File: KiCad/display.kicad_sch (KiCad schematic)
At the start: 34 parts, among them IC2 R1200N001A-TR-FE, J3 Conn_01x34_NHD_18, Q4 DMG2302U, U6 LT1963AxST-2.5

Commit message: Create Revision 0.0.1
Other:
- company: (none) -> ETH Zurich: Center for Project Based Learning
- title: (none) -> STDC: Display
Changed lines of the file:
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@@
 	(generator_version "9.0")
 	(paper "A4")
+	(title_block
+		(title "STDC: Display")
+		(date "2026-03-05")
+		(rev "0.0.1")
+		(company "ETH Zurich: Center for Project Based Learning")
+	)
 	(rectangle
 		(start 71.12 15.24)

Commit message: Added some TODOs, fixed some TODOs
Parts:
- renumbered C14 to C48, C48 to C49
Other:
- note added: "TODO: Check Peak Saturation Current through L4"
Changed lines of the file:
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@@
 		)
 	)
+	(text "TODO: Check Peak \nSaturation Current\nthrough L4"
+		(exclude_from_sim no)
+		(at 242.57 95.758 0)
+		(effects
+			(font
+				(size 1.27 1.27)
+			)
+		)
+	)
 	(text "1.8V with Power Decoupling\nfor Display VDDIO"
 		(exclude_from_sim no)
@@
 	(text "V_{out}=V_{FB}×(R1+R2)/R1\nV_{FB} = 1.238\n(17/1.238)=13.73\nR2=12.73×R1\n(200k/16k)=12.5"
 		(exclude_from_sim no)
-		(at 242.316 84.582 0)
+		(at 242.062 83.058 0)
 		(effects
 			(font
@@
 		(on_board yes)
 		(dnp no)
-		(property "Reference" "C14"
+		(property "Reference" "C48"
 			(at 212.598 80.518 0)
 			(effects
@@
 			(project ""
 				(path "/643c756f-a801-466b-9148-7370ee6a5e00/603cffac-84d5-485b-bf95-e3987997ef84"
-					(reference "C14")
+					(reference "C48")
 					(unit 1)
 				)
@@
 		(on_board yes)
 		(dnp no)
-		(property "Reference" "C48"
+		(property "Reference" "C49"
 			(at 222.504 80.518 0)
 			(effects
@@
 			(project "STDC"
 				(path "/643c756f-a801-466b-9148-7370ee6a5e00/603cffac-84d5-485b-bf95-e3987997ef84"
-					(reference "C48")
+					(reference "C49")
 					(unit 1)
 				)

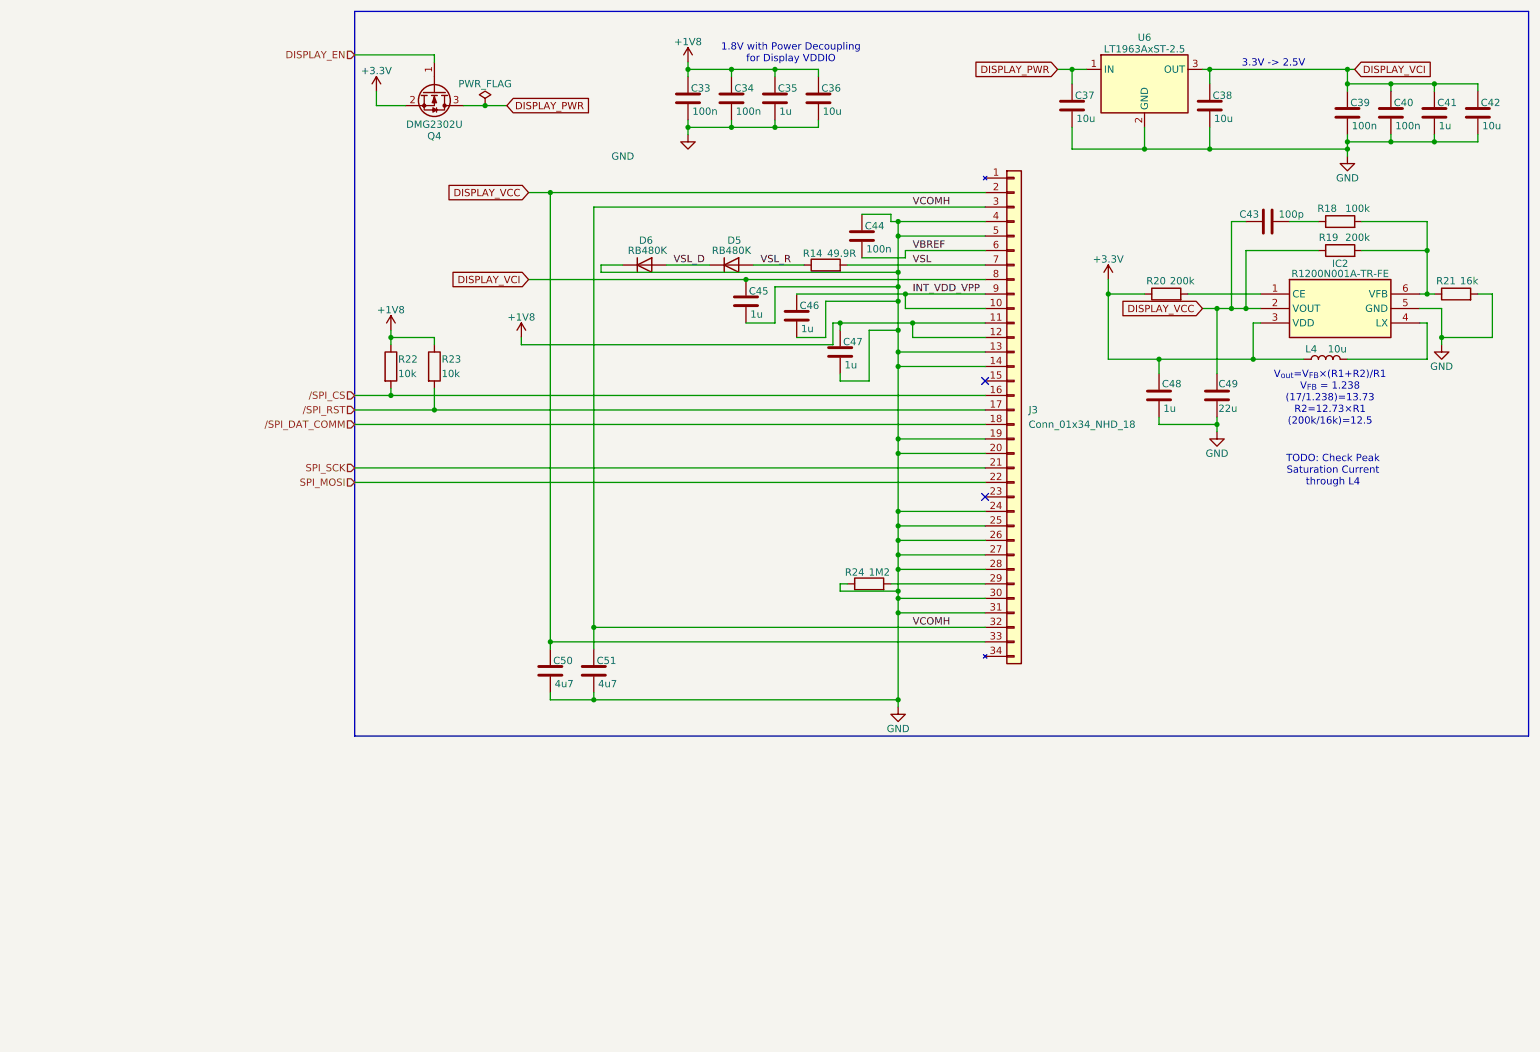
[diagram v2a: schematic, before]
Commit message: Testing connectors, SPI2 pinout, reannotate
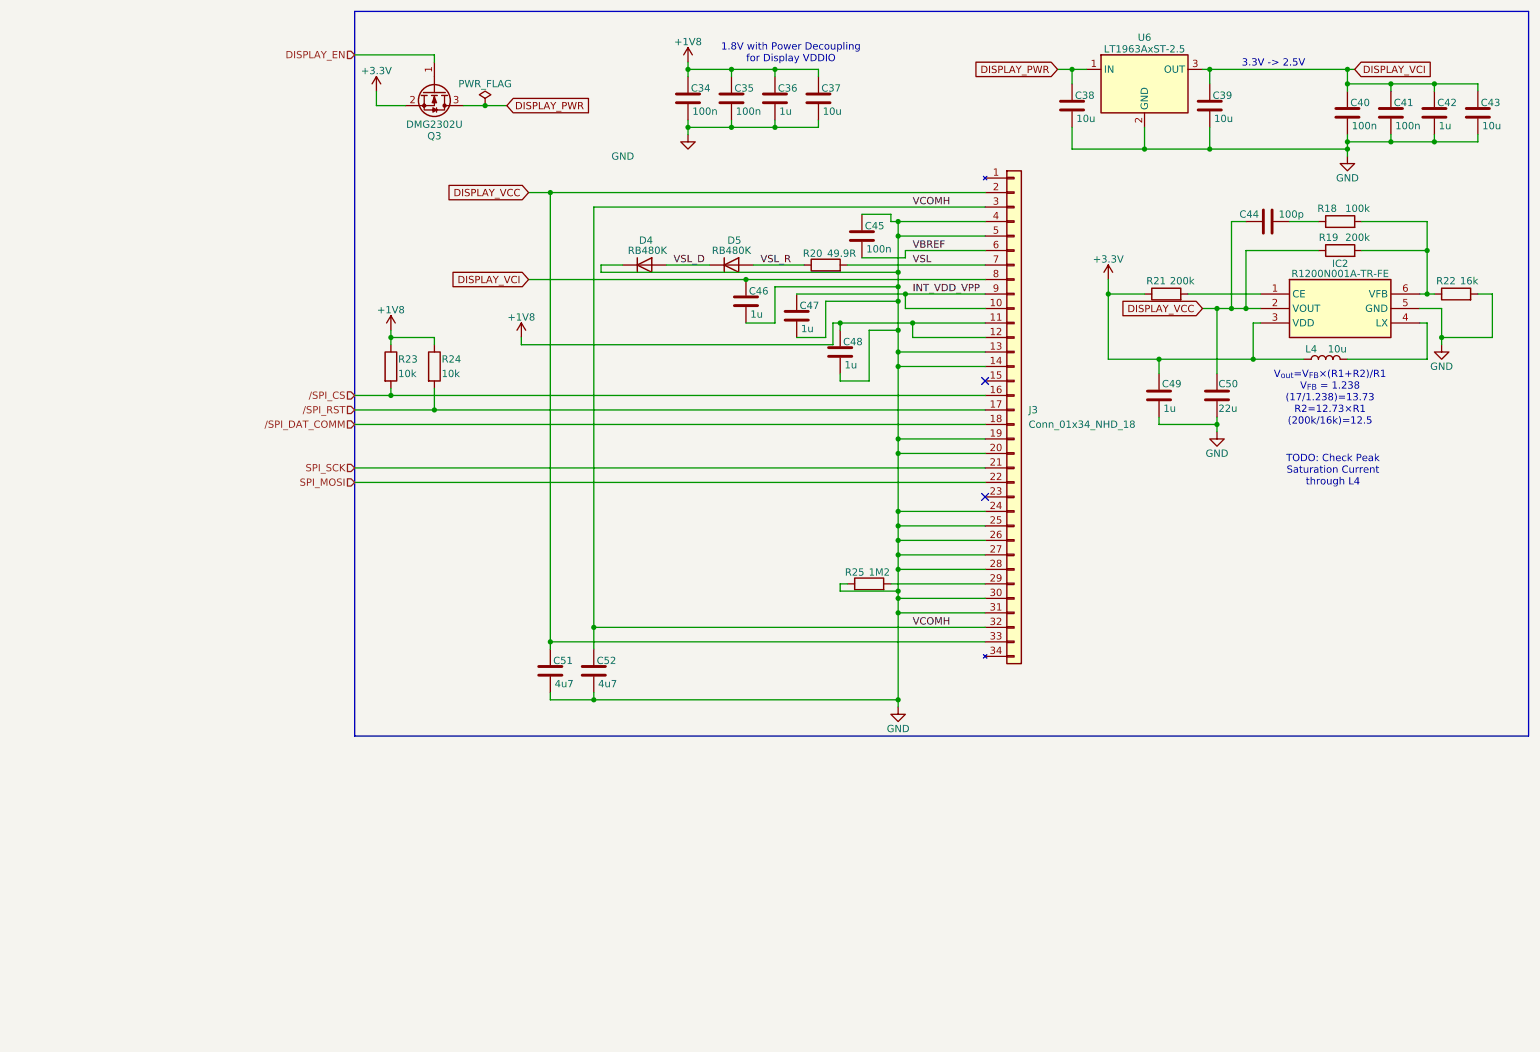
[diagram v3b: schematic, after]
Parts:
- renumbered C33 to C34, C34 to C35, C35 to C36, C36 to C37, C37 to C38, C38 to C39, C39 to C40, C40 to C41, C41 to C42, C42 to C43, C43 to C44, C44 to C45, C45 to C46, C46 to C47, C47 to C48, C48 to C49, C49 to C50, C50 to C51, C51 to C52, D6 to D4, Q4 to Q3, R14 to R20, R20 to R21, R21 to R22, R22 to R23, R23 to R24, R24 to R25

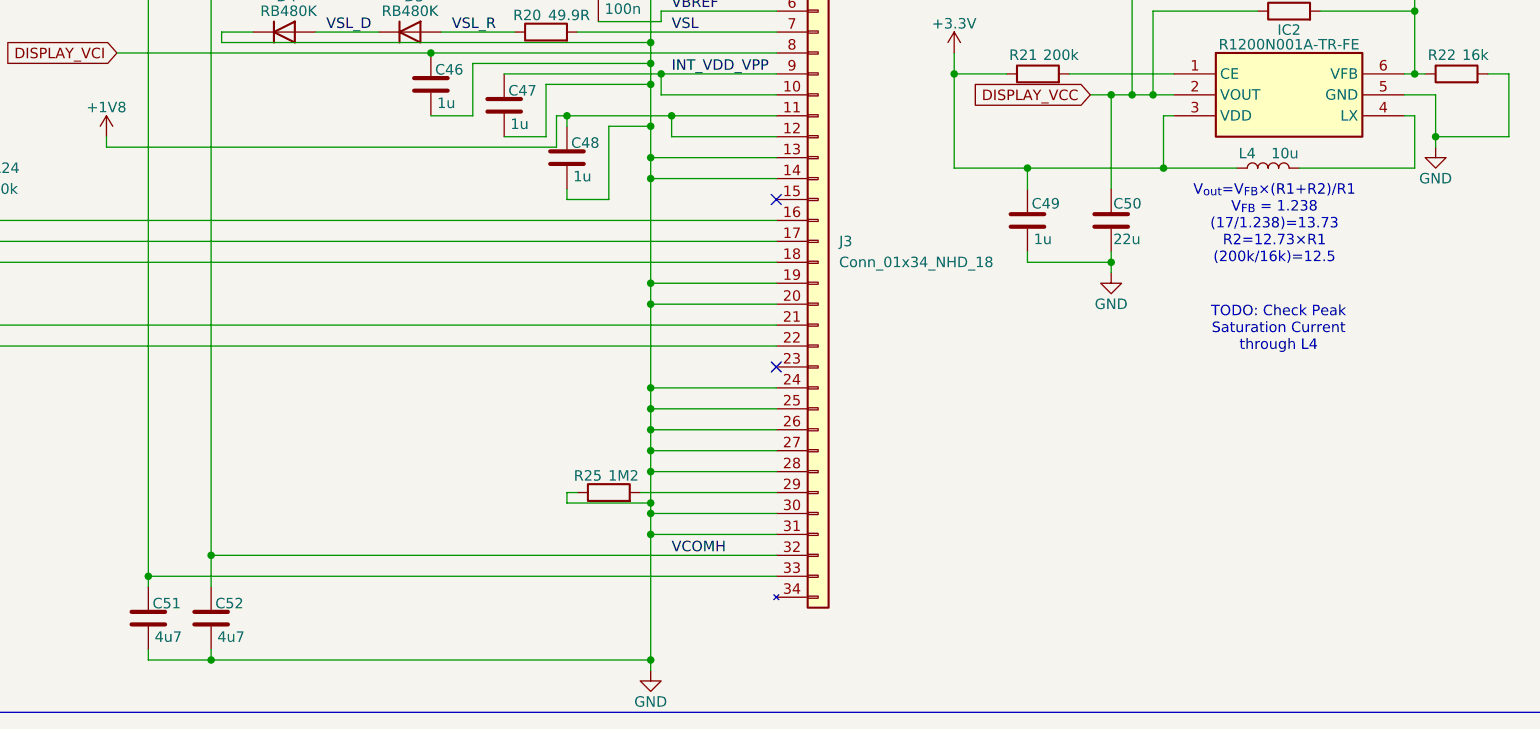
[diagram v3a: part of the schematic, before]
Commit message: Calculate saturation current for coils and add comments
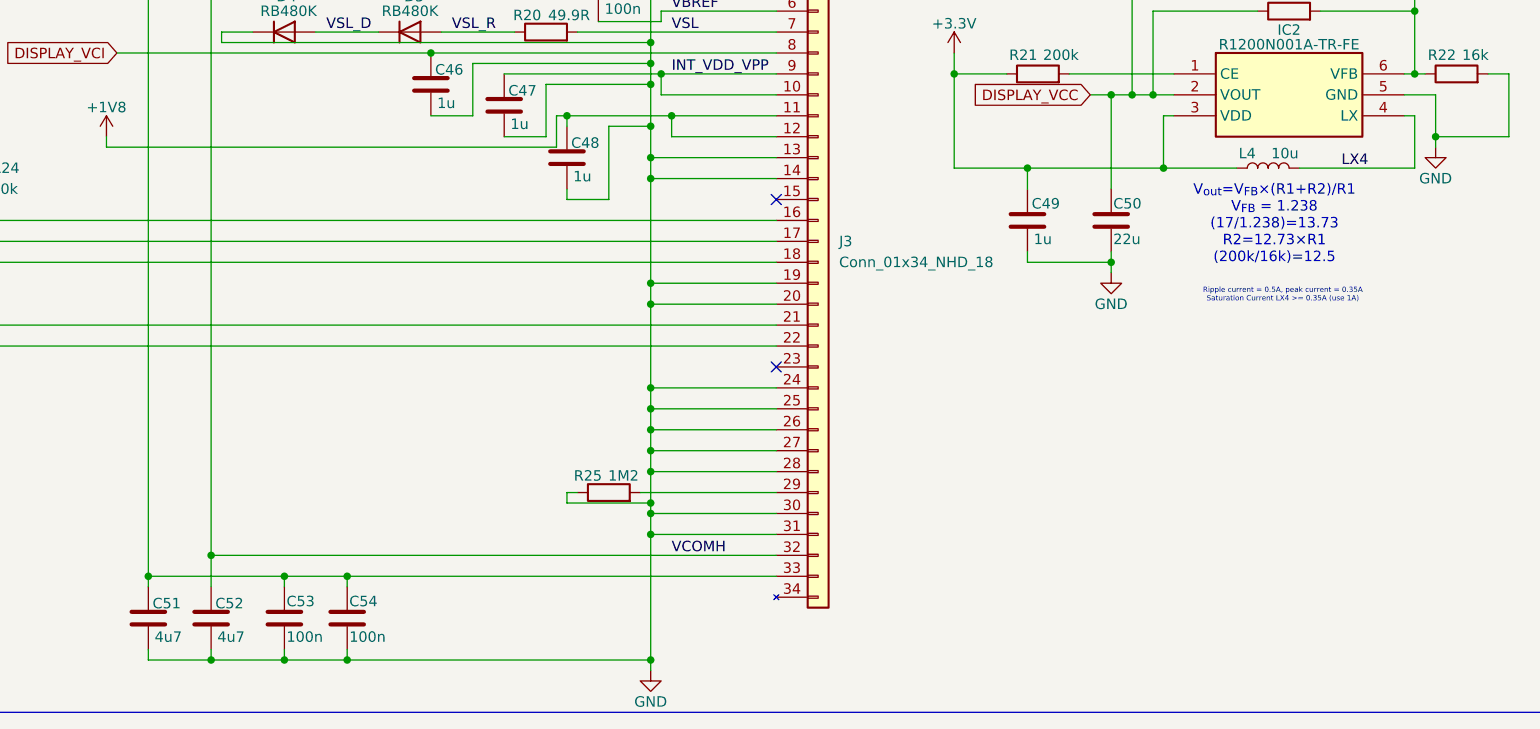
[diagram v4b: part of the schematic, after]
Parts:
- added C53, C54: 100n, Capacitor_SMD:C_0402_1005Metric, symbol Device:C
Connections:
- net DISPLAY_VCC: now also C53.1, C54.1
- net GND: now also C53.2, C54.2
- net LX4: now reaches IC2.4 (LX), L4.2
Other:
- note added: "Ripple current = 0.5A, peak current = 0.35A Saturation Current LX4 >= 0.35A (use 1A)"
- note removed: "TODO: Check Peak Saturation Current through L4"

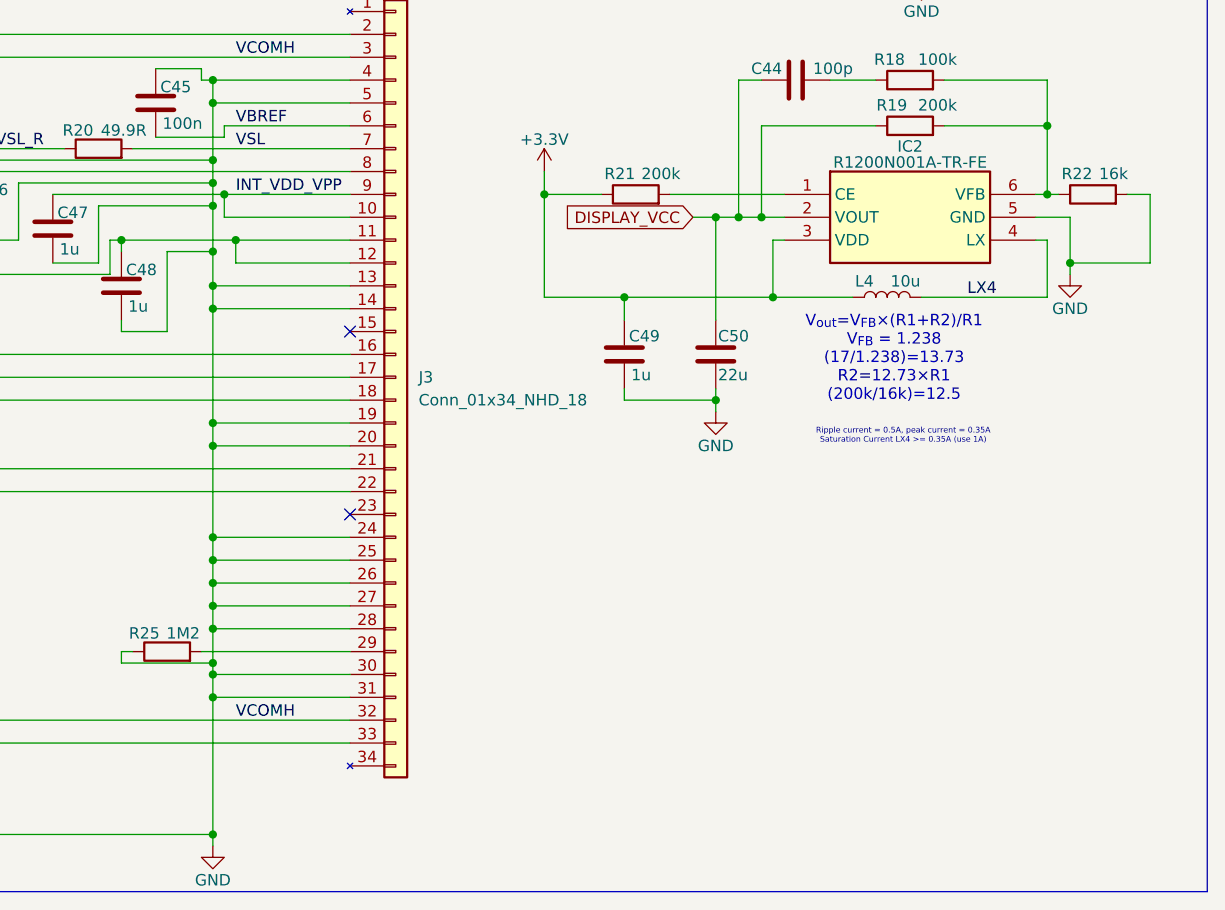
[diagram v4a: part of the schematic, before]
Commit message: Fix display Rs to fix 17V reference and consolidate BOM
And add more info to R_{IREF}
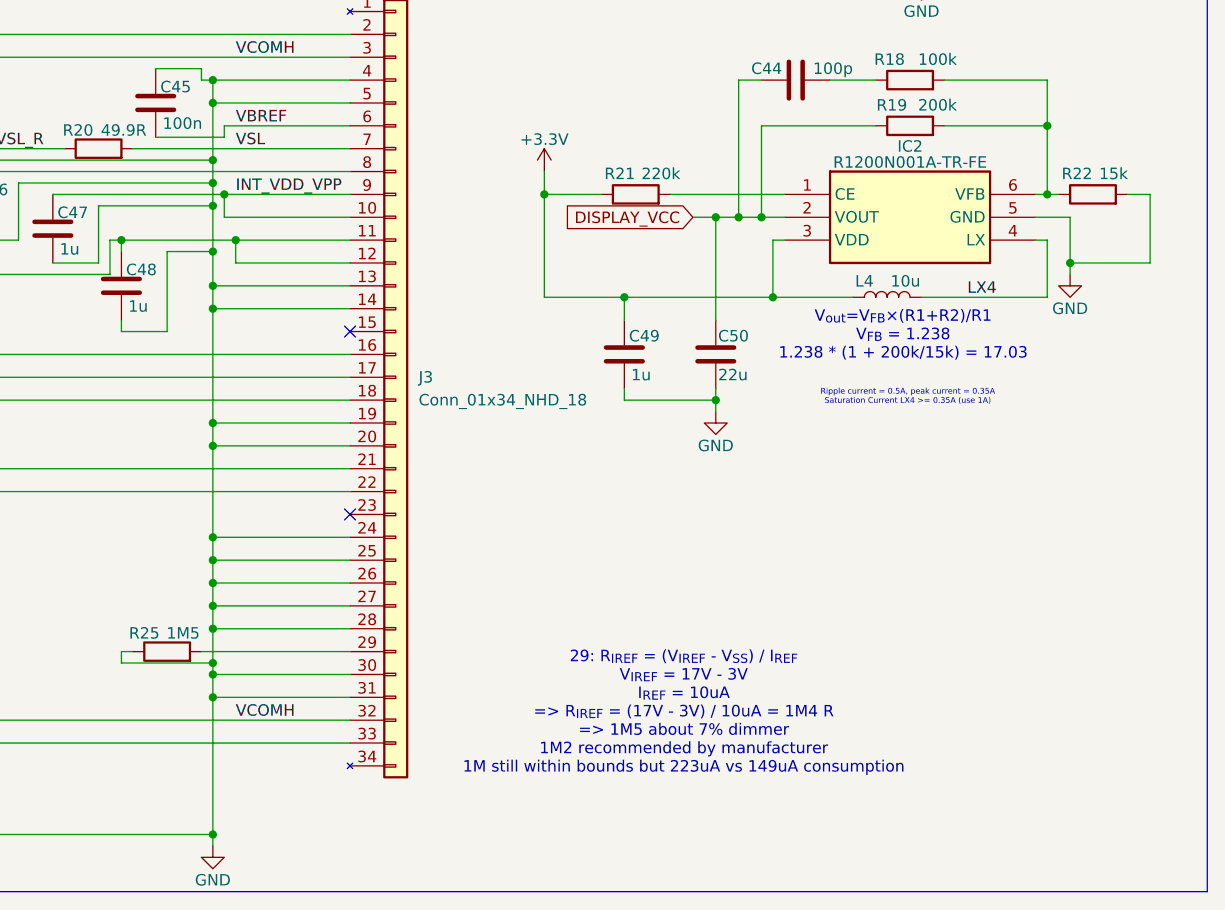
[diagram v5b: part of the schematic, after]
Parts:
- R21: value 200k -> 220k
- R22: value 16k -> 15k
- R25: value 1M2 -> 1M5
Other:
- note added: "29: R_{IREF} = (V_{IREF} - V_{SS}) / I_{REF} V_{IREF} = 17V - 3V I_{REF} = 10uA => R_{IREF} = (17V - 3V) / 10uA = 1M4 R => 1M5 about 7% dimmer 1M2 recommended by manufacturer 1M still within bounds but 223uA vs 149uA consumption"
- note added: "V_{out}=V_{FB}×(R1+R2)/R1 V_{FB} = 1.238 1.238 * (1 + 200k/15k) = 17.03"
- note removed: "V_{out}=V_{FB}×(R1+R2)/R1 V_{FB} = 1.238 (17/1.238)=13.73 R2=12.73×R1 (200k/16k)=12.5"
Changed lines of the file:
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@@
 	(text "Ripple current = 0.5A, peak current = 0.35A\nSaturation Current LX4 >= 0.35A (use 1A)"
 		(exclude_from_sim no)
-		(at 243.078 91.694 0)
+		(at 243.586 87.376 0)
 		(effects
 			(font
@@
 		)
 	)
-	(text "V_{out}=V_{FB}×(R1+R2)/R1\nV_{FB} = 1.238\n(17/1.238)=13.73\nR2=12.73×R1\n(200k/16k)=12.5"
+	(text "V_{out}=V_{FB}×(R1+R2)/R1\nV_{FB} = 1.238\n1.238 * (1 + 200k/15k) = 17.03"
 		(exclude_from_sim no)
-		(at 242.062 83.058 0)
+		(at 243.078 80.518 0)
 		(effects
 			(font
@@
 		)
 	)
+	(text "29: R_{IREF} = (V_{IREF} - V_{SS}) / I_{REF}\nV_{IREF} = 17V - 3V\nI_{REF} = 10uA\n=> R_{IREF} = (17V - 3V) / 10uA = 1M4 R\n=> 1M5 about 7% dimmer\n1M2 recommended by manufacturer\n1M still within bounds but 223uA vs 149uA consumption"
+		(exclude_from_sim no)
+		(at 218.694 122.428 0)
+		(effects
+			(font
+				(size 1.27 1.27)
+			)
+		)
+	)
 	(junction
 		(at 166.37 63.5)
@@
 			)
 		)
-		(property "Value" "16k"
+		(property "Value" "15k"
 			(at 266.446 62.484 90)
 			(effects
@@
 			)
 		)
-		(property "Value" "200k"
+		(property "Value" "220k"
 			(at 216.154 62.484 90)
 			(effects
@@
 			)
 		)
-		(property "Value" "1M2"
+		(property "Value" "1M5"
 			(at 163.068 113.538 90)
 			(effects
